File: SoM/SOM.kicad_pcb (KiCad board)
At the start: 6 copper layers, 67.6 x 50 mm, 135 parts, among them J1 SODIMM-200_Split, Q1 BC847, Q2 BC847, U1 CCGM1A1, U2 MX25V8035F, U3 74LVC2G53, U4 MPM3833C, U5 MPM3833C, X1 ECS-5032MV

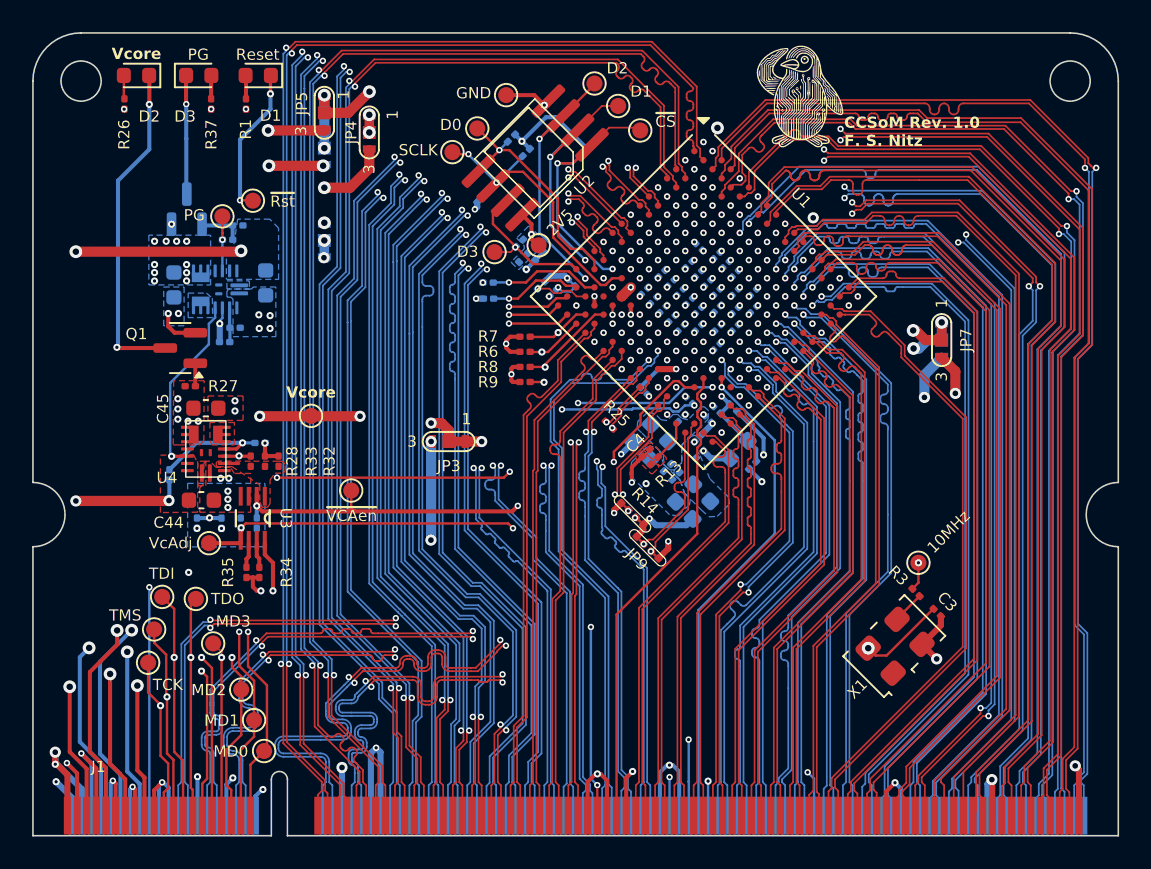
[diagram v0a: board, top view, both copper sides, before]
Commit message: Created Version with 0402 components
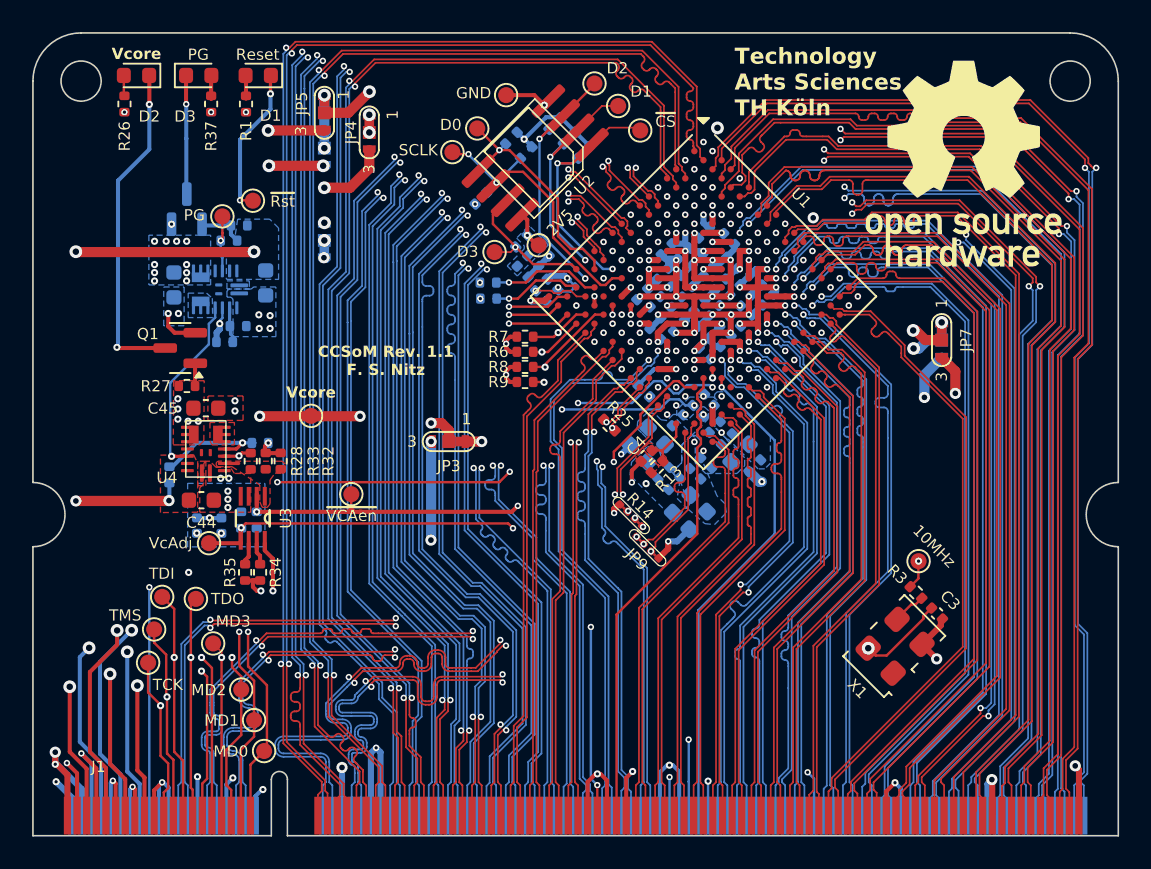
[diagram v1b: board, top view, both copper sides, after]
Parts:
- C1, C11, C12, C13, C14, C15, C16, C17, C18, C19, C2, C21, C22, C23, C24, C25, C26, C27, C28, C29, C3, C30, C31, C32, C33, C34, C35, C36, C37, C38, C39, C4, C40, C41, C42, C43, C5, C7, C8, C9: footprint Capacitor_SMD:C_0201_0603Metric -> Capacitor_SMD:C_0402_1005Metric
- R1, R10, R11, R12, R13, R15, R16, R17, R18, R19, R2, R20, R21, R22, R23, R24, R25, R26, R27, R28, R29, R3, R30, R31, R32, R33, R34, R35, R36, R37, R38, R39, R4, R40, R41, R5, R6, R7, R8, R9: footprint Resistor_SMD:R_0201_0603Metric -> Resistor_SMD:R_0402_1005Metric
- log2: moved to F.Cu
- moved log1 28.8 mm to (140.4, 68.2)
- moved log2 27.1 mm to (176.6, 63.5), turned to 0 degrees
- moved C35 7.12 mm to (164.4, 71.9), turned to 45 degrees
- moved C14 6.22 mm to (157.4, 74.1), turned to -45 degrees
- moved C28 5.85 mm to (162.0, 68.2), turned to 135 degrees
- moved C13 5.79 mm to (156.6, 71.6)
- moved C27 5.47 mm to (158.1, 72.1), turned to -45 degrees
- moved C38 4.42 mm to (162.2, 69.6), turned to -45 degrees
- moved C34 4.37 mm to (161.8, 74.5), turned to -135 degrees
- moved C37 4.11 mm to (160.5, 75.3), turned to 135 degrees
- moved C40 3.96 mm to (163.0, 71.3), turned to 135 degrees
- moved C36 3.57 mm to (160.0, 70.1), turned to -45 degrees
- moved C16 3.55 mm to (157.9, 70.3), turned to -135 degrees
- moved C31 2.68 mm to (157.4, 72.7), turned to 135 degrees
- moved C33 2.54 mm to (163.1, 73.2), turned to -135 degrees
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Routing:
- net Vcore: track 67.3 -> 113.4 mm, vias 38 -> 30
- net GND: track 121.6 -> 160.5 mm, vias 120 -> 103
- net Net-(U1G-VDD_PLL): track 5.46 -> 0.02 mm
- net /FPGA_Top_Module/FPGA_IO_Config/VDD_EA: track 10.0 -> 11.7 mm
- net /FPGA_Top_Module/FPGA_IO_Config/VDD_NA: track 28.6 -> 30.3 mm, vias 6 -> 5
- net /FPGA_Top_Module/FPGA_IO_Config/VDD_EB: track 6.68 -> 8.38 mm, vias 6 -> 5
- net /FPGA_Top_Module/FPGA_IO_Config/VDD_NB: track 36.5 -> 38.2 mm, vias 7 -> 6
- net /FPGA_Top_Module/FPGA_IO_Config/VDD_WB: track 19.1 -> 20.5 mm
- net /FPGA_Top_Module/WC7_N: track 79.9 -> 81.3 mm
- net /FPGA_Top_Module/FPGA_IO_Config/VDD_SA: track 16.4 -> 17.6 mm
- net /FPGA_Top_Module/SA8_N: track 30.3 -> 31.2 mm
- net /FPGA_Top_Module/~{VcAen}: track 36.8 -> 37.6 mm
- net Net-(U1A-SER_RTERM1): track 2.56 -> 3.36 mm
- net /FPGA_Top_Module/SA4_N: track 33.6 -> 34.3 mm
- net /FPGA_Top_Module/NA6_P: track 60.5 -> 59.7 mm
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- added copper zone on B.Cu, net Net-(U1G-VDD_PLL)
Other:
- board text added: "CCSoM Rev. 1.1 F. S. Nitz"
- board text removed: "CCSoM Rev. 1.0 F. S. Nitz"
